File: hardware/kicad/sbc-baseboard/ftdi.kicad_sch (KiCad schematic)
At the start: 22 parts, among them J9 FTDI header, U501 FT231XS

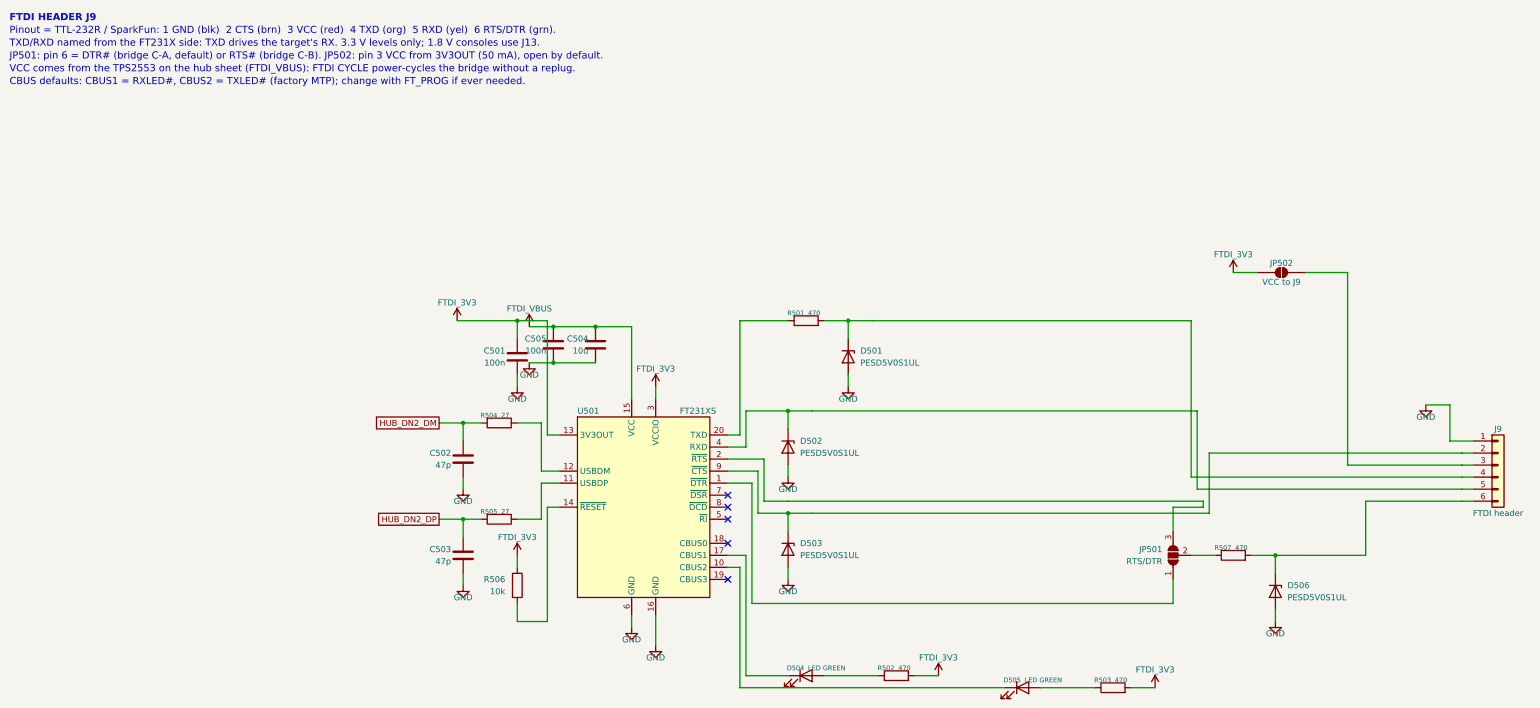
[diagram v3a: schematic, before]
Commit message: USB 2.0 differential pairs named for the router; USB net class; ports aligned
Every USB 2.0 data net is now <base>_P / <base>_N, the suffixes KiCad's PCB
editor pairs up: J1_D, J3_D, PORT1_D..PORT4_D on the receptacle side of each
ESD array; HUB_UP and HUB_DN1..HUB_DN7 at the hub; K64_USB and FTDI_USB at the
chips. All 15 pairs are complete with D+ on _P. The project file gains a USB
net class assigned by pattern (differential geometry to be set from the
stackup). The labels sit at wire ends with their text along the pair's own
wire; routes now run their last leg into a side pin as one wire so a label at
the pin end owns the stretch (Conn join=False keeps a shared stub where two
routes meet at one pin). The USB-A receptacles and their switches move down
1.27 mm so the pairs run straight from the ESD arrays, and the port ESD arrays
move left to make room for the labels. Netlist membership unchanged (356
nets); ERC, geometry, connectivity, layout and reproducibility gates all
clean.

Co-Authored-By: Claude Fable 5.1 <noreply@anthropic.com>
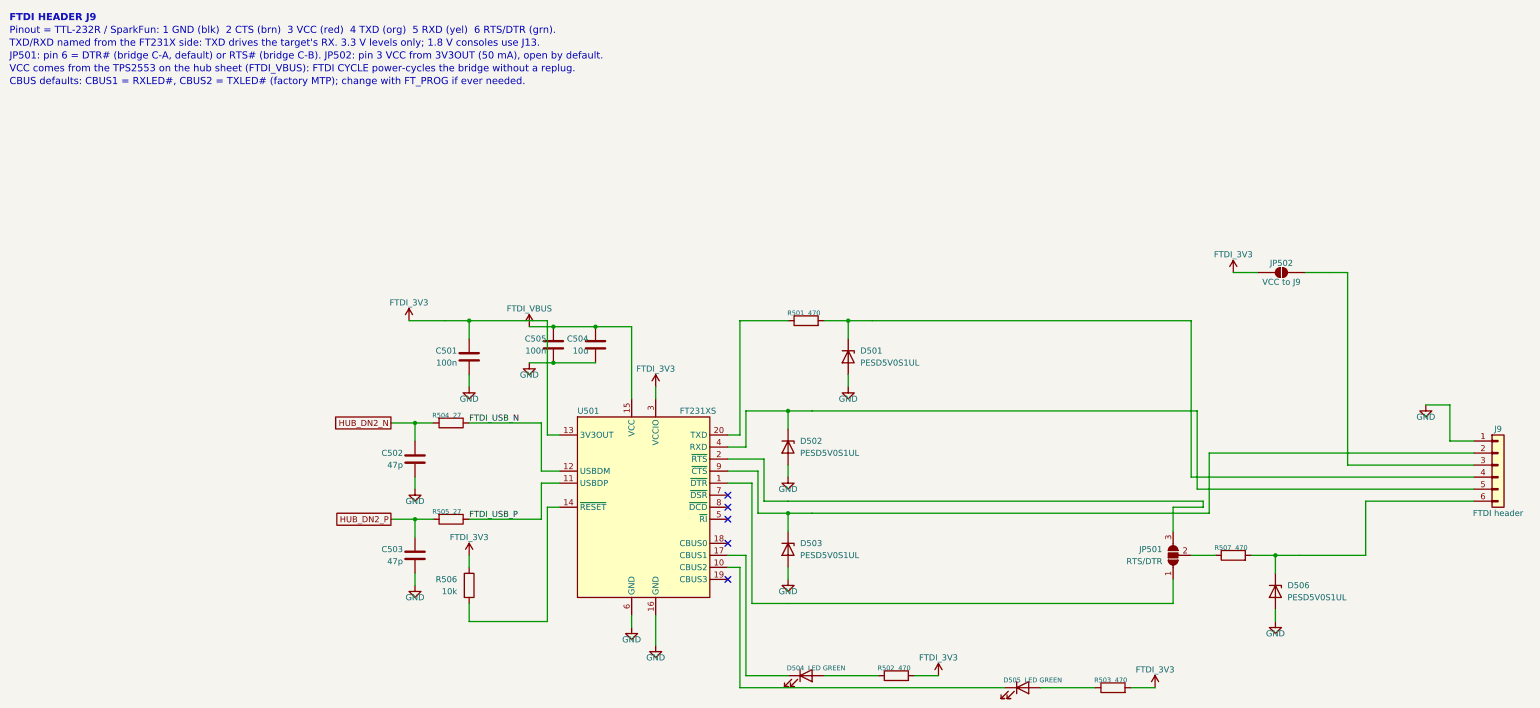
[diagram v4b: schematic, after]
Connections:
- net FTDI_USB_P: now reaches R505.1, U501.11 (USBDP)
- net FTDI_USB_N: now reaches R504.1, U501.12 (USBDM)
- net HUB_DN2_DM renamed HUB_DN2_N
- net HUB_DN2_DP renamed HUB_DN2_P
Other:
- moved on the sheet: C501, C502, C503, R504, R505, R506

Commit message: Nothing drawn over anything else; FTDI Friend header; DAPLink per FRDM-K64F; 90 ohm USB class
Geometry gate now also reports two wires sharing a stretch, and is at zero on
every sheet. Routes into a stacked connector from one side take staggered
columns and rows; the signal relays are flipped so COM meets the header's
first pin without crossings; the opto-isolator moves above the passthrough
wires and taps the relay's COM lane; a tag before a route ends at the route's
target; routes into joined pins end at the join; the K64's VREGIN diode taps
the VBUS lane beside the ESD's stub; symbol mirrors are applied after
rotation, as KiCad does.

FT231X: the 3V3OUT lane stays on its pin row with its capacitor far out, clear
of the VCC decoupling; J9 mirrors the Adafruit FTDI Friend (VCC 5 V and pin 6
RTS by default on bridged solder jumpers; the first pass had left J9's VCC on
an open jumper only).

DAPLink K20, verified against DAPLink k20dx and the FRDM-K64F OpenSDA circuit:
PTC7 (SWDIO_IN) joins the SWDIO net, 33 R series resistors on the K20's USB
pair (K20_USB_P/N), notes and spec questions 12 and 14 resolved.

USB net class: 0.35 mm / 0.20 mm for 90 ohm on Advanced Circuits' standard
4-layer 62 mil stackup (spec section 8a). ERC 0, geometry 0, merges 0, layout
0, builds reproducible.

Co-Authored-By: Claude Fable 5.1 <noreply@anthropic.com>
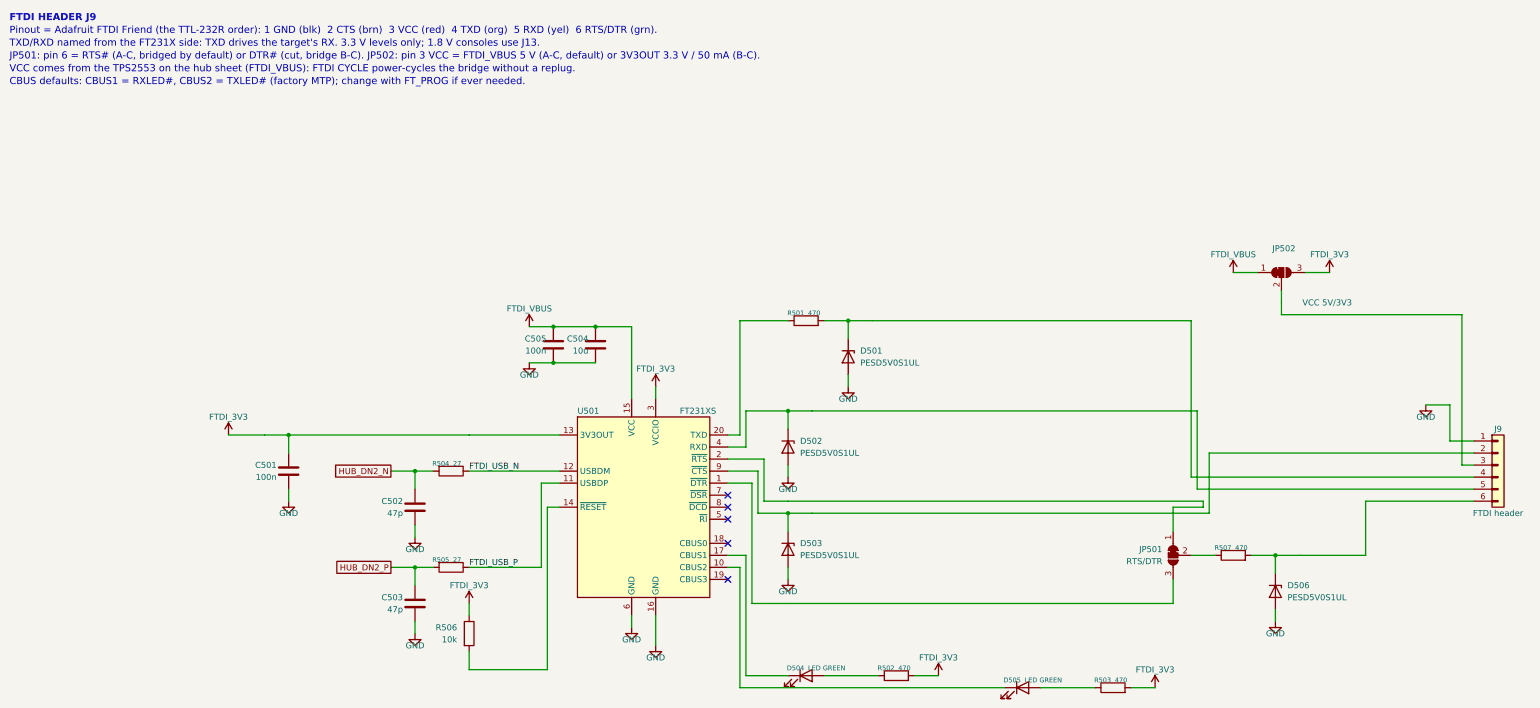
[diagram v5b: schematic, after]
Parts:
- JP501: footprint Jumper:SolderJumper-3_P1.3mm_Open_RoundedPad1.0x1.5mm -> Jumper:SolderJumper-3_P1.3mm_Bridged12_RoundedPad1.0x1.5mm; symbol Jumper:SolderJumper_3_Open -> Jumper:SolderJumper_3_Bridged12
- JP502: value VCC to J9 -> VCC 5V/3V3; footprint Jumper:SolderJumper-2_P1.3mm_Open_RoundedPad1.0x1.5mm -> Jumper:SolderJumper-3_P1.3mm_Bridged12_RoundedPad1.0x1.5mm; symbol Jumper:SolderJumper_2_Open -> Jumper:SolderJumper_3_Bridged12
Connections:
- net FTDI_3V3: now also JP502.3 (B); no longer JP502.1 (A)
- net FTDI_VBUS: now also JP502.1 (A)
- net at JP501.1 (A): now also U501.2 (~{RTS}); no longer U501.1 (~{DTR})
- net at JP501.3 (B): now also U501.1 (~{DTR}); no longer U501.2 (~{RTS})
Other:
- note added: "JP501: pin 6 = RTS# (A-C, bridged by default) or DTR# (cut, bridge B-C). JP502: pin 3 VCC = FTDI_VBUS 5 V (A-C, default) or 3V3OUT 3.3 V / 50 mA (B-C)."
- note added: "Pinout = Adafruit FTDI Friend (the TTL-232R order): 1 GND (blk) 2 CTS (brn) 3 VCC (red) 4 TXD (org) 5 RXD (yel) 6 RTS/DTR (grn)."
- note removed: "JP501: pin 6 = DTR# (bridge C-A, default) or RTS# (bridge C-B). JP502: pin 3 VCC from 3V3OUT (50 mA), open by default."
- note removed: "Pinout = TTL-232R / SparkFun: 1 GND (blk) 2 CTS (brn) 3 VCC (red) 4 TXD (org) 5 RXD (yel) 6 RTS/DTR (grn)."
- moved on the sheet: C501, C502, C503, R504, R505, R506
